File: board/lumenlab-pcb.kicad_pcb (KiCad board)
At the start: 2 copper layers, 22 parts, among them J1 2.1mm Barrel Jack, U1 MP2338, U2 AMS1117

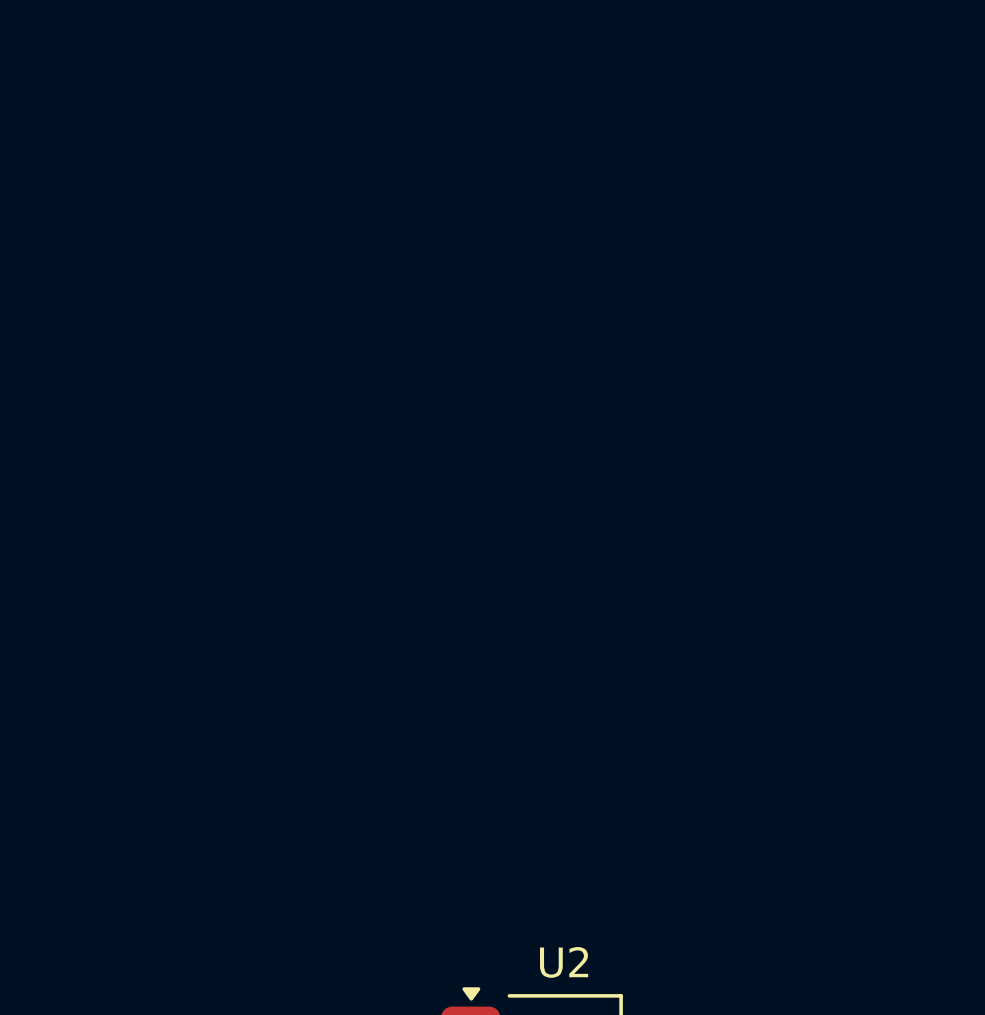
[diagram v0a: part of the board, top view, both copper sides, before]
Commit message: Add ESP32 to schematic
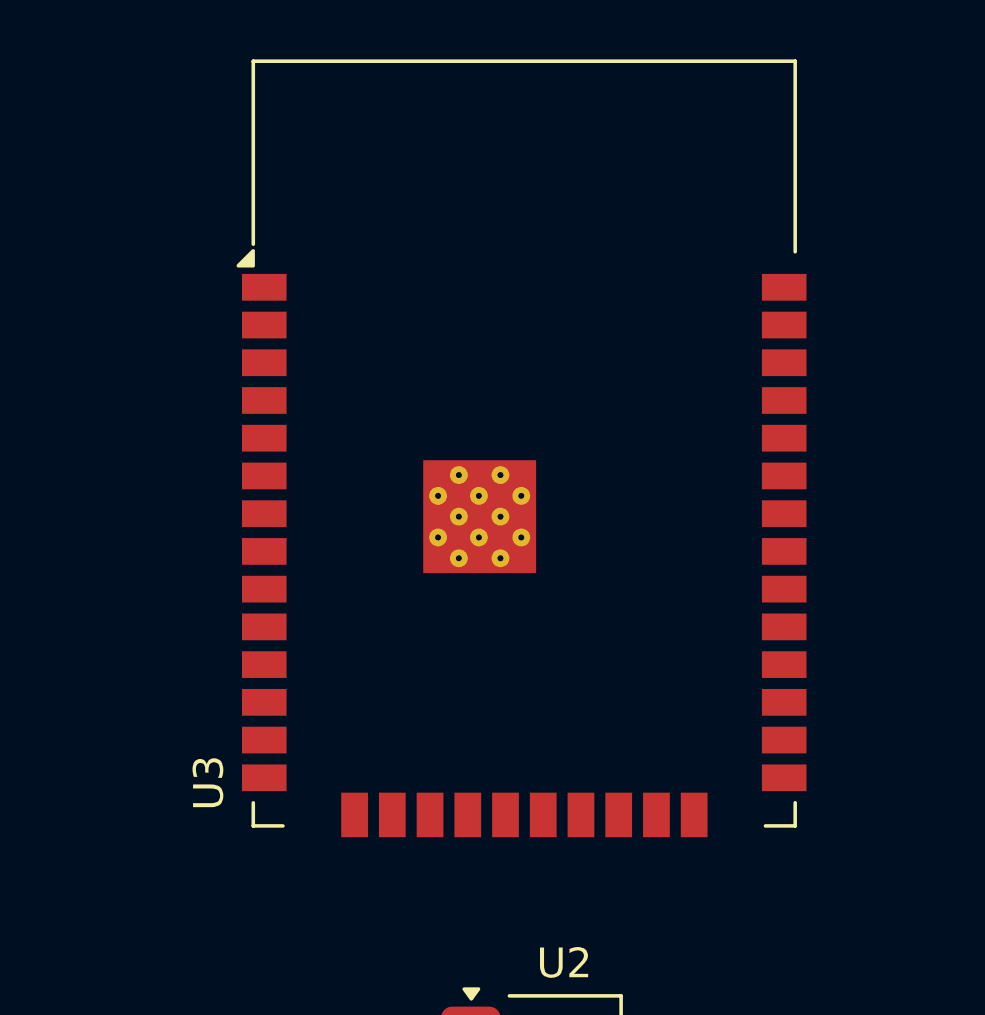
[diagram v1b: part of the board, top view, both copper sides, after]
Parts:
- added U3: ESP32-WROOM-32D, RF_Module:ESP32-WROOM-32D, F.Cu at (149.8, 54.2)

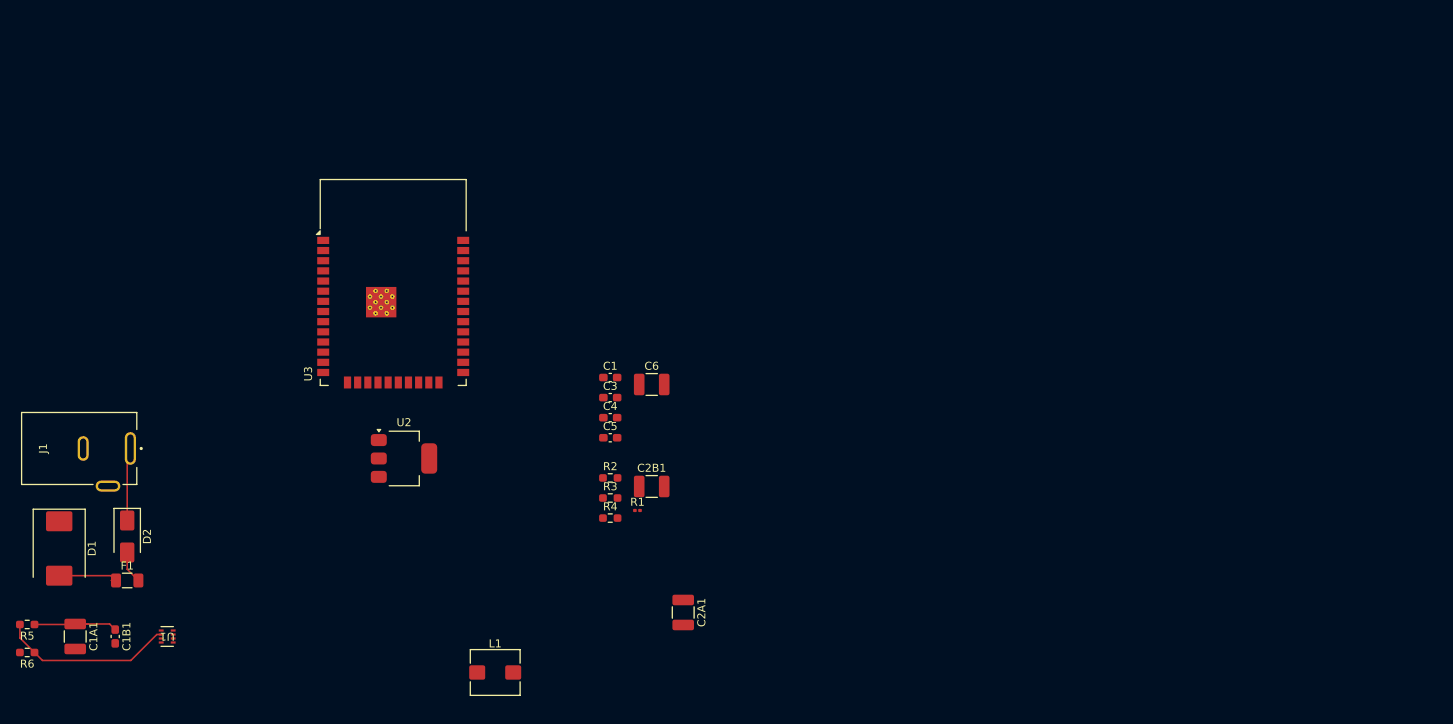
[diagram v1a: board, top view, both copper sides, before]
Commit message: Add custom symbols, footprints, and 3D models
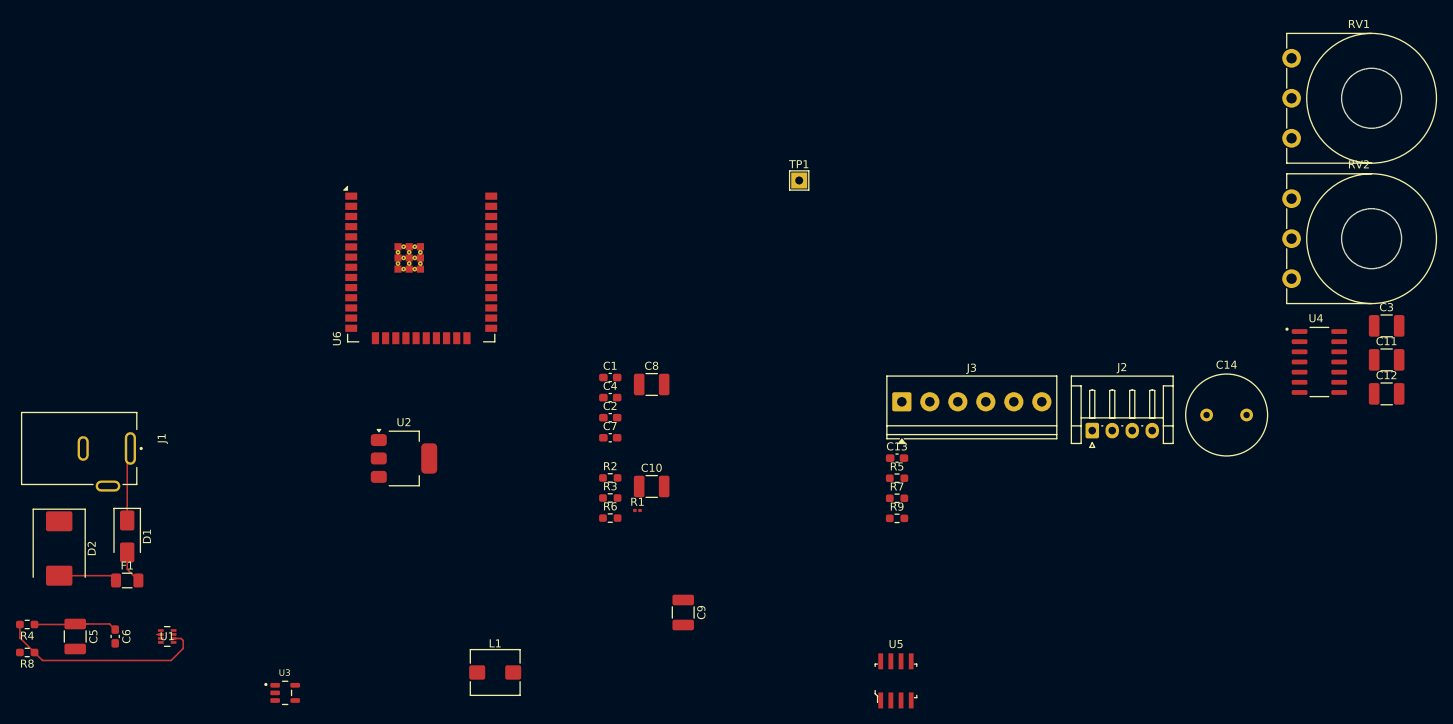
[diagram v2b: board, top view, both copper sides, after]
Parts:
- added C11: 10uF, Capacitor_SMD:C_1210_3225Metric_Pad1.33x2.70mm_HandSolder, F.Cu at (273.9, 60.9)
- added C12: 0.1uF, Capacitor_SMD:C_1210_3225Metric_Pad1.33x2.70mm_HandSolder, F.Cu at (273.9, 65.2)
- added C13: 0.1uF, Capacitor_SMD:C_0603_1608Metric_Pad1.08x0.95mm_HandSolder, F.Cu at (212.7, 73.2)
- added C14: 1000uF, Capacitor_THT:C_Radial_D10.0mm_H20.0mm_P5.00mm, F.Cu at (251.4, 67.8)
- added C3: 0.1uF, Capacitor_SMD:C_1210_3225Metric_Pad1.33x2.70mm_HandSolder, F.Cu at (273.9, 56.7)
- added J2: Conn_01x04_Pin, Connector_JST:JST_EH_S4B-EH_1x04_P2.50mm_Horizontal, F.Cu at (237.1, 69.8)
- added J3: Screw_Terminal_01x06, TerminalBlock_Phoenix:TerminalBlock_Phoenix_PT-1,5-6-3.5-H_1x06_P3.50mm_Horizontal, F.Cu at (213.3, 66.2)
- added R5: 330, Resistor_SMD:R_0603_1608Metric_Pad0.98x0.95mm_HandSolder, F.Cu at (212.7, 75.7)
- added R7: 100, Resistor_SMD:R_0603_1608Metric_Pad0.98x0.95mm_HandSolder, F.Cu at (212.7, 78.2)
- added R9: 1K, Resistor_SMD:R_0603_1608Metric_Pad0.98x0.95mm_HandSolder, F.Cu at (212.7, 80.7)
- added RV1: 10K LIN, Potentiometer_THT:Potentiometer_Piher_T-16L_Single_Vertical_Hole, F.Cu at (262.1, 33.2)
- added RV2: 10K LOG, Potentiometer_THT:Potentiometer_Piher_T-16L_Single_Vertical_Hole, F.Cu at (262.1, 50.8)
- added TP1: TestPoint, TestPoint:TestPoint_THTPad_2.0x2.0mm_Drill1.0mm, F.Cu at (200.5, 38.5)
- added U4: SN74HC14N, 2_Vendor_SN74HC14N:sn74hc14dr, F.Cu at (265.5, 61.2)
- added U5: 1_Custom_LM386MX-1_NOPB, digikey-footprints:SOIC-8_W3.9mm, F.Cu at (212.6, 101.0)
- added U6: ESP32-WROOM-32E, RF_Module:ESP32-WROOM-32E, F.Cu at (153.2, 45.7)
- C7: renamed from C5; value 10uF -> 4.7uF
- C8: renamed from C6; value 22uF -> 4.7uF
- J1: footprint 54-00129:TENSILITY_54-00129 -> 2_Vendor_BarrelJack:2_Vendor_BarrelJack
- U1: footprint MP2338:SOT583_MP2338_MNP -> 2_Vendor_MP2338:MP2338_MNP-M
- U2: value AMS1117 -> AP7361C-33E
- U3: value ESP32-WROOM-32D -> SN74AHC1G125DBVR; footprint RF_Module:ESP32-WROOM-32D -> 2_Vendor_SN74AHC1G125:SN74AHC1G125
- moved U3 50.2 mm to (136.2, 102.5)
- turned U1 to 0 degrees
- renumbered C2B1 to C10, C4 to C2, C3 to C4, C1A1 to C5, C1B1 to C6, C2A1 to C9, D2 to D1, D1 to D2, R5 to R4, R4 to R6, R6 to R8
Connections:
- D2 pad 1: GND -> +12V
- D2 pad 2: +12V -> GND
- R3 pad 1: /BUCK_FB -> Net-(C1-Pad1)
- U2 pad 1: GND -> +5V
- U2 pad 2: +3.3V -> GND
- U2 pad 3: +5V -> +3.3V
- U3 pad 2: +3.3V -> Net-(U3-A)
- U3 pad 3: unconnected-(U3-EN-Pad3) -> GND
- U3 pad 4: unconnected-(U3-SENSOR_VP-Pad4) -> Net-(U3-Y)
- U3 pad 5: unconnected-(U3-SENSOR_VN-Pad5) -> Net-(U3-VCC)
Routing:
- net /BUCK_EN: track 21.9 -> 26.2 mm
- net +12V: track 29.1 -> 29.6 mm

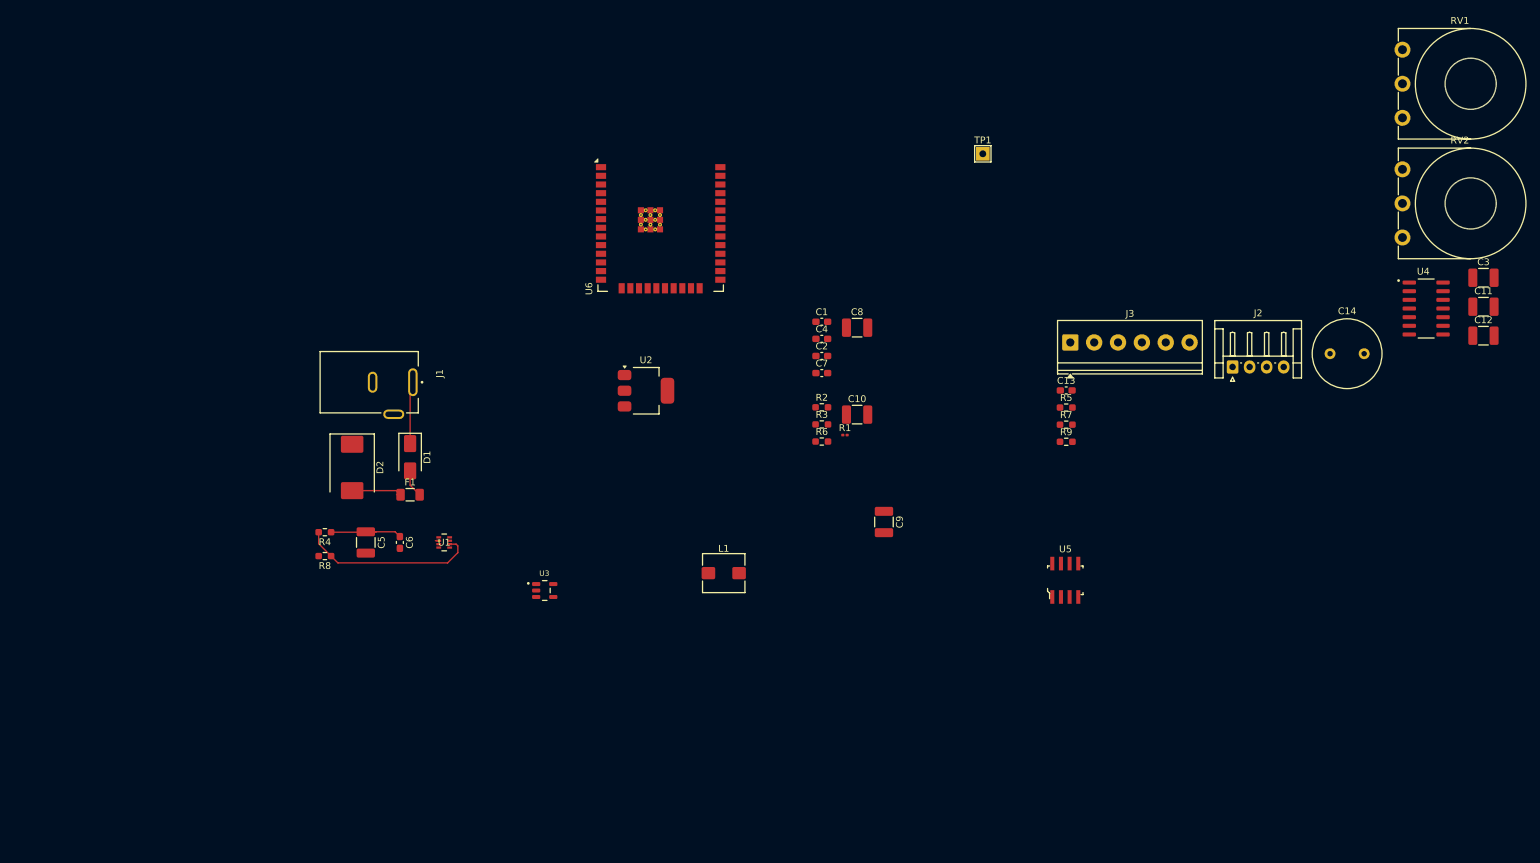
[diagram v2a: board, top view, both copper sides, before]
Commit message: Resolve conflicting GPIO ADC pin 34 for navigation left button
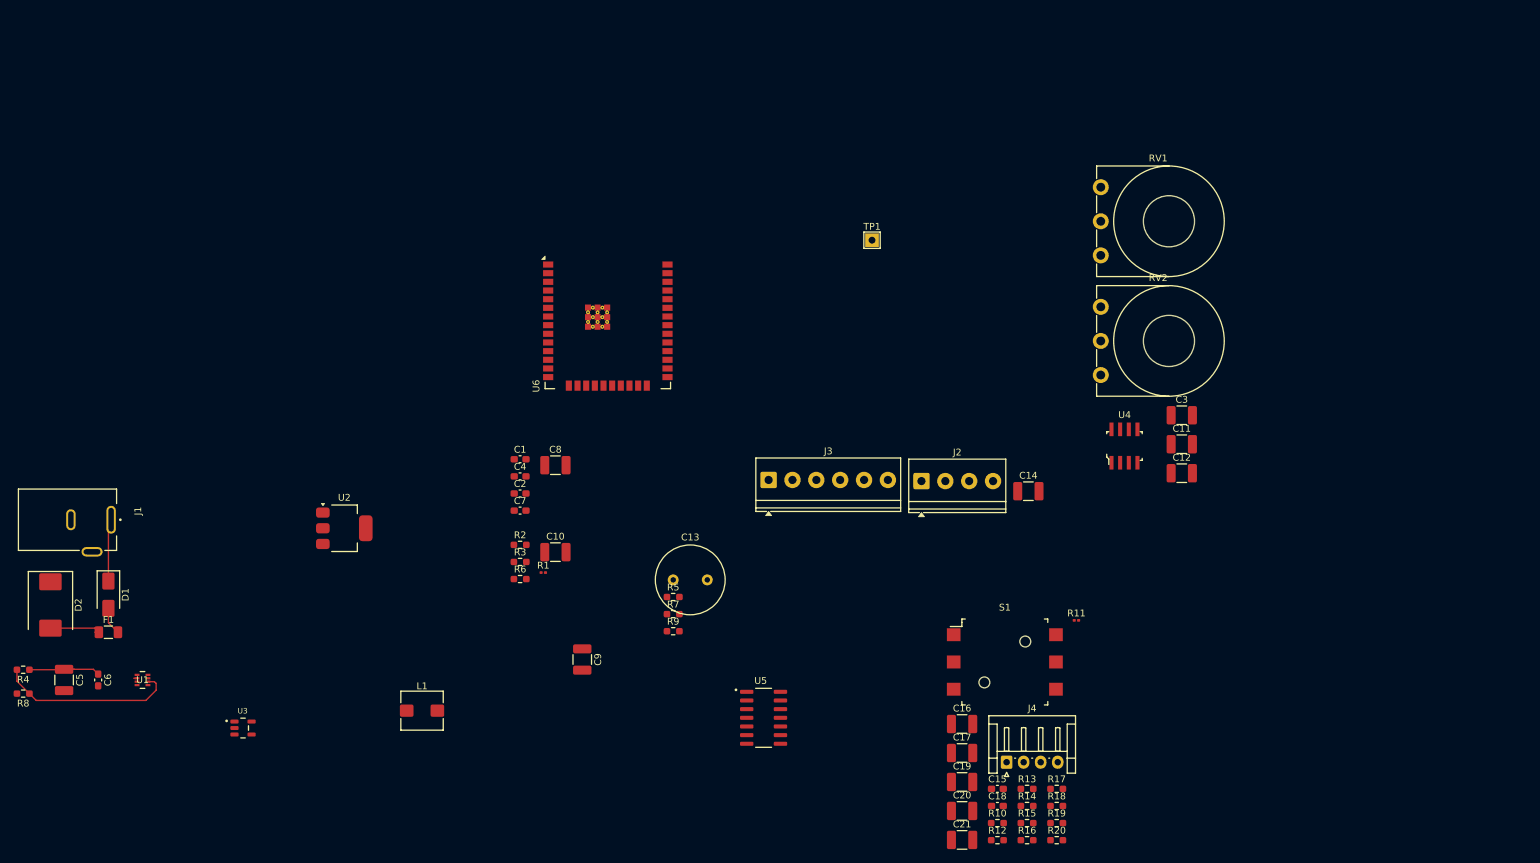
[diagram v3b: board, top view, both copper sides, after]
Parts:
- added C15: 0.1uF, Capacitor_SMD:C_0603_1608Metric_Pad1.08x0.95mm_HandSolder, F.Cu at (202.6, 131.6)
- added C16: 0.05uF, Capacitor_SMD:C_1210_3225Metric_Pad1.33x2.70mm_HandSolder, F.Cu at (197.5, 122.1)
- added C17: 0.1uF, Capacitor_SMD:C_1210_3225Metric_Pad1.33x2.70mm_HandSolder, F.Cu at (197.5, 126.4)
- added C18: 0.1uF, Capacitor_SMD:C_0603_1608Metric_Pad1.08x0.95mm_HandSolder, F.Cu at (202.6, 134.2)
- added C19: 0.1uF, Capacitor_SMD:C_1210_3225Metric_Pad1.33x2.70mm_HandSolder, F.Cu at (197.5, 130.6)
- added C20: 0.1uF, Capacitor_SMD:C_1210_3225Metric_Pad1.33x2.70mm_HandSolder, F.Cu at (197.5, 134.9)
- added C21: 0.1uF, Capacitor_SMD:C_1210_3225Metric_Pad1.33x2.70mm_HandSolder, F.Cu at (197.5, 139.1)
- added J4: Conn_01x04_Pin, Connector_JST:JST_EH_S4B-EH_1x04_P2.50mm_Horizontal, F.Cu at (204.0, 127.7)
- added R10: 47K, Resistor_SMD:R_0603_1608Metric_Pad0.98x0.95mm_HandSolder, F.Cu at (202.6, 136.7)
- added R11: 90.9K, Resistor_SMD:R_0201_0603Metric, F.Cu at (214.2, 106.9)
- added R12: 100, Resistor_SMD:R_0603_1608Metric_Pad0.98x0.95mm_HandSolder, F.Cu at (202.6, 139.2)
- added R13: 47K, Resistor_SMD:R_0603_1608Metric_Pad0.98x0.95mm_HandSolder, F.Cu at (207.0, 131.6)
- added R14: 100, Resistor_SMD:R_0603_1608Metric_Pad0.98x0.95mm_HandSolder, F.Cu at (207.0, 134.2)
- added R15: 100, Resistor_SMD:R_0603_1608Metric_Pad0.98x0.95mm_HandSolder, F.Cu at (207.0, 136.7)
- added R16: 1K, Resistor_SMD:R_0603_1608Metric_Pad0.98x0.95mm_HandSolder, F.Cu at (207.0, 139.2)
- added R17: 100, Resistor_SMD:R_0603_1608Metric_Pad0.98x0.95mm_HandSolder, F.Cu at (211.3, 131.6)
- added R18: 100, Resistor_SMD:R_0603_1608Metric_Pad0.98x0.95mm_HandSolder, F.Cu at (211.3, 134.2)
- added R19: 47K, Resistor_SMD:R_0603_1608Metric_Pad0.98x0.95mm_HandSolder, F.Cu at (211.3, 136.7)
- added R20: 47K, Resistor_SMD:R_0603_1608Metric_Pad0.98x0.95mm_HandSolder, F.Cu at (211.3, 139.2)
- added S1: JS5208, digikey-footprints:Switch_Nav_12.4x12.4mm_SMD_JS5208, F.Cu at (203.7, 113.0)
- C11: value 10uF -> 0.1uF
- C12: value 0.1uF -> 10uF
- C13: value 0.1uF -> 1000uF; footprint Capacitor_SMD:C_0603_1608Metric_Pad1.08x0.95mm_HandSolder -> Capacitor_THT:C_Radial_D10.0mm_H20.0mm_P5.00mm
- C14: value 1000uF -> 0.1uF; footprint Capacitor_THT:C_Radial_D10.0mm_H20.0mm_P5.00mm -> Capacitor_SMD:C_1210_3225Metric_Pad1.33x2.70mm_HandSolder
- J2: value Conn_01x04_Pin -> Screw_Terminal_01x04; footprint Connector_JST:JST_EH_S4B-EH_1x04_P2.50mm_Horizontal -> TerminalBlock_Phoenix:TerminalBlock_Phoenix_PT-1,5-4-3.5-H_1x04_P3.50mm_Horizontal
- R5: value 330 -> 10K
- R6: value 10K -> 330
- R9: value 1K -> 47K
- U4: value SN74HC14N -> 1_Custom_LM386MX-1_NOPB; footprint 2_Vendor_SN74HC14N:sn74hc14dr -> digikey-footprints:SOIC-8_W3.9mm
- U5: value 1_Custom_LM386MX-1_NOPB -> SN74HC14DR; footprint digikey-footprints:SOIC-8_W3.9mm -> 2_Vendor_SN74HC14N:sn74hc14dr
- moved R7 64.0 mm to (155.1, 106.0)
- moved C13 64.0 mm to (155.1, 101.0)
- moved R5 64.0 mm to (155.1, 103.5)
- moved R9 64.0 mm to (155.1, 108.5)
- moved C1 48.6 mm to (132.6, 83.3)
- moved C10 48.6 mm to (137.8, 96.9)
- moved C11 48.6 mm to (229.7, 81.1)
- moved C12 48.6 mm to (229.7, 85.3)
- moved C14 48.6 mm to (207.2, 88.0)
- moved C2 48.6 mm to (132.6, 88.3)
- moved C3 48.6 mm to (229.7, 76.8)
- moved C4 48.6 mm to (132.6, 85.8)
- moved C5 48.6 mm to (65.8, 115.7)
- moved C6 48.6 mm to (70.8, 115.7)
- moved C7 48.6 mm to (132.6, 90.8)
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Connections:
- C11 pad 1: GND -> /DEBOUNCE_UP
- C11 pad 2: +3.3V -> GND
- C14 pad 1: +12V -> +3.3V
- C3 pad 1: +5V -> Net-(U3-VCC)
- C3 pad 2: Net-(U3-VCC) -> +5V
- J2 pad 1: unconnected-(J2-Pin_1-Pad1) -> +12V
- J2 pad 2: unconnected-(J2-Pin_2-Pad2) -> +12V
- J2 pad 3: unconnected-(J2-Pin_3-Pad3) -> GND
- J2 pad 4: unconnected-(J2-Pin_4-Pad4) -> GND
- R5 pad 1: /LED_DIN -> /BUCK_PG
- R5 pad 2: Net-(U3-Y) -> +5V
- R6 pad 1: /BUCK_PG -> /LED_DIN
- R6 pad 2: +5V -> Net-(U3-Y)
- R9 pad 1: /ESP32_GPIO34 -> +3.3V
- R9 pad 2: Net-(R9-Pad2) -> /DEBOUNCE_UP
- RV1 pad 2: Net-(R9-Pad2) -> Net-(R16-Pad2)
- RV2 pad 1: unconnected-(RV2-Pad1) -> GND
- U4 pad 2: unconnected-(U4-1Y-Pad2) -> GND
- U4 pad 3: unconnected-(U4-2A-Pad3) -> /AMP_IN
- U4 pad 4: unconnected-(U4-2Y-Pad4) -> GND
- U4 pad 5: unconnected-(U4-3A-Pad5) -> Net-(C16-Pad1)
- U4 pad 6: unconnected-(U4-3Y-Pad6) -> +5V
- U4 pad 7: GND -> unconnected-(U4-Pad7)
- U5 pad 1: unconnected-(U5-GAIN-Pad1) -> /DEBOUNCE_UP
- U5 pad 2: unconnected-(U5-Pad2) -> Net-(U5-1Y)
- U5 pad 3: /AMP_IN -> /DEBOUNCE_DOWN
- U5 pad 4: unconnected-(U5-GND-Pad4) -> Net-(U5-2Y)
- U5 pad 5: unconnected-(U5-OUTPUT-Pad5) -> /DEBOUNCE_LEFT
- U5 pad 6: unconnected-(U5-SIGNAL-Pad6) -> Net-(U5-3Y)
- U5 pad 7: unconnected-(U5-BYPASS-Pad7) -> GND
- U5 pad 8: unconnected-(U5-GAIN-Pad8) -> Net-(U5-4Y)
- U6 pad 12: unconnected-(U6-IO27-Pad12) -> /ESP32_GPIO27
- U6 pad 33: unconnected-(U6-IO21-Pad33) -> /ESP32_GPIO21
- U6 pad 7: unconnected-(U6-IO35-Pad7) -> /ESP32_GPIO35
- U6 pad 8: unconnected-(U6-IO32-Pad8) -> /ESP32_GPIO32
- U6 pad 9: unconnected-(U6-IO33-Pad9) -> /ESP32_GPIO33
